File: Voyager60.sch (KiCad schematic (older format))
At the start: 261 parts, among them Q1 2N7002, SW1 5.2x5.2mm, U1 ATmega32U4-MU, U2 PRTR5V0U2X, Y1 16Mhz

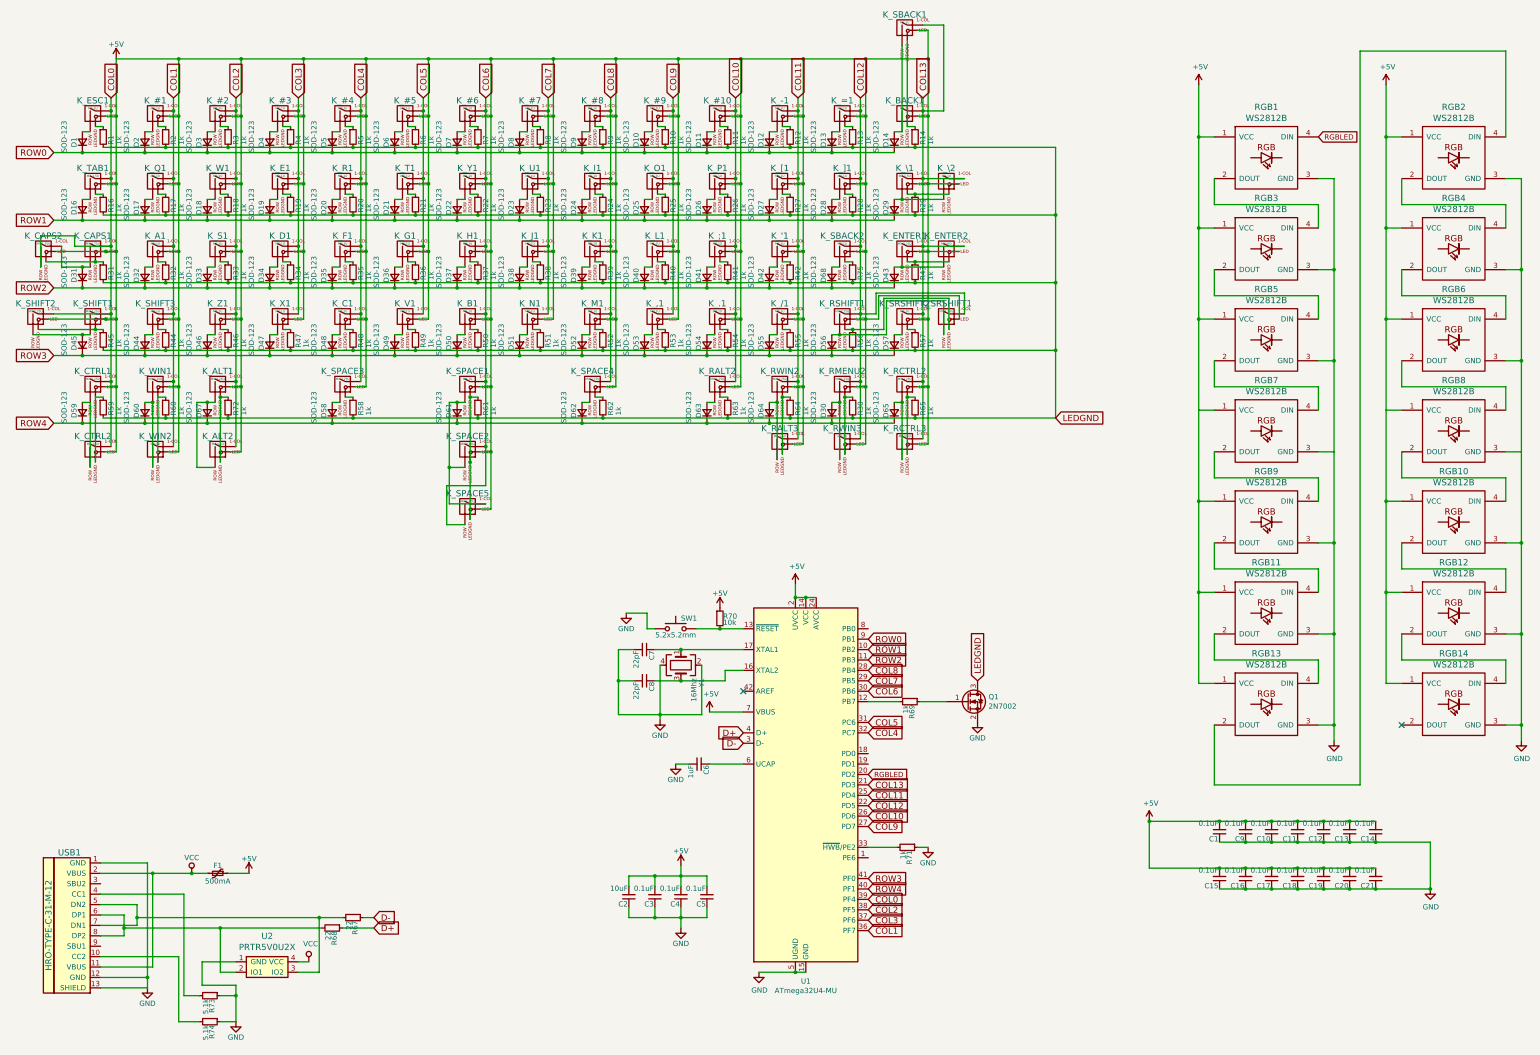
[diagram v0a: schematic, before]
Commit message: 65% variant of voyager60
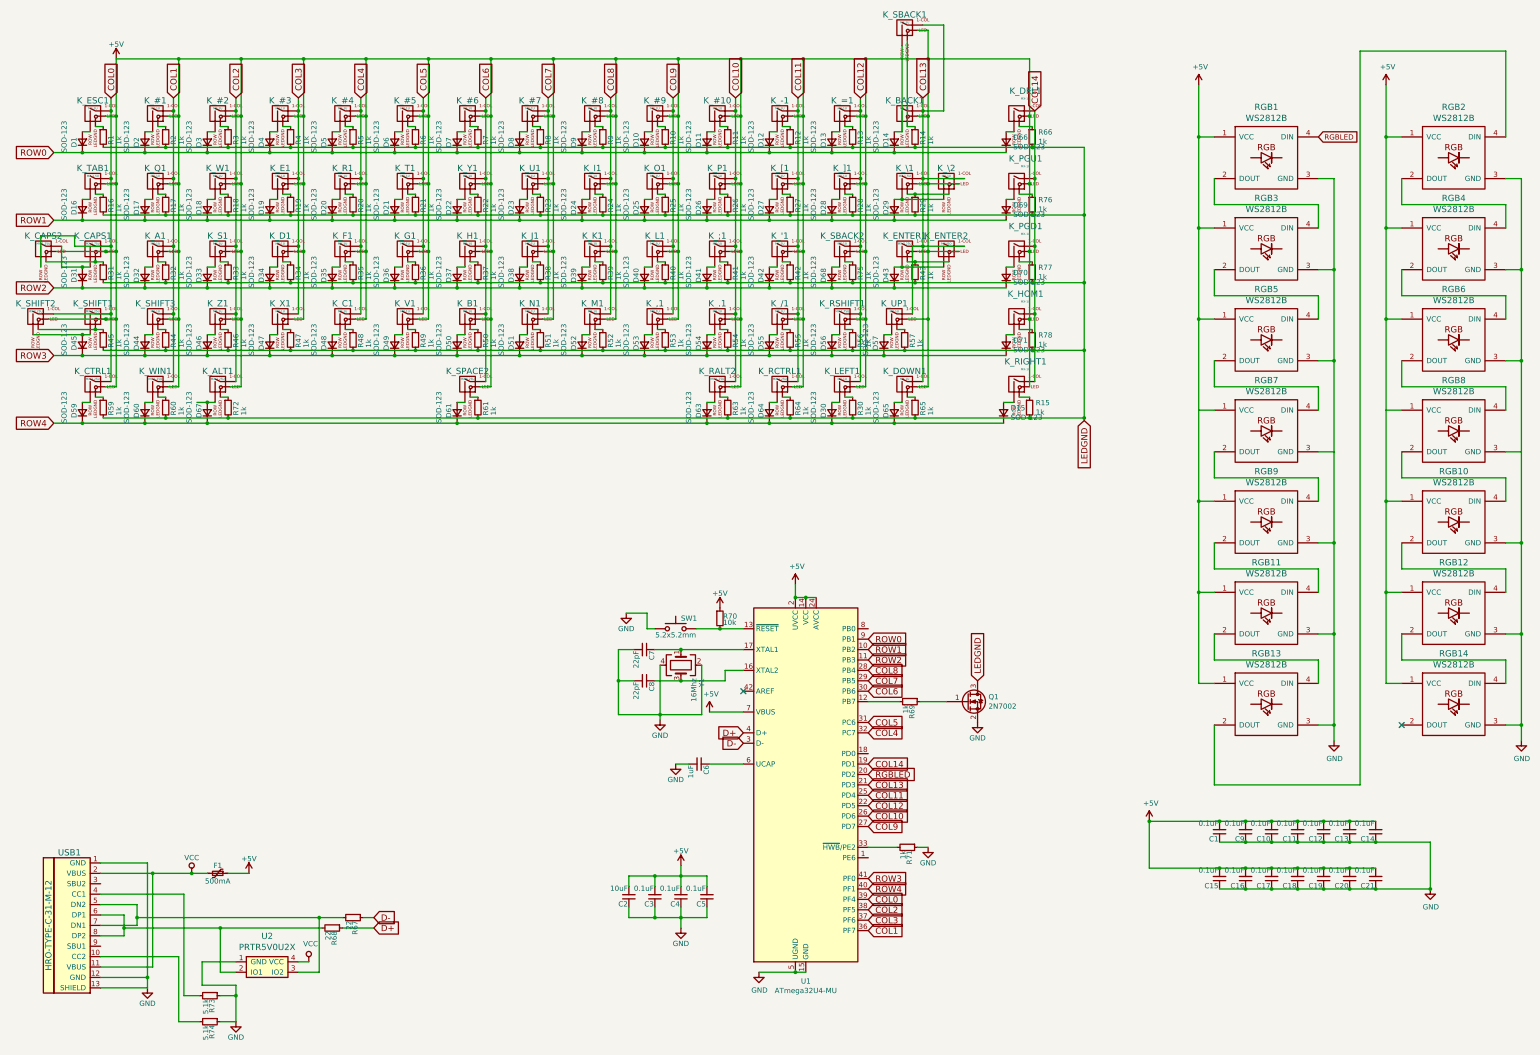
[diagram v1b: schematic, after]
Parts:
- removed D58, D62: SOD-123, Diodes_SMD:D_SOD-123, symbol Device:D_Small
- removed K_ALT2, K_CTRL2, K_RALT3, K_RCTRL3: MX-1.5U, MX_Alps_Hybrid:MX-1.5U-FLIPPED, symbol MX_Alps_Hybrids:MX-1U
- removed K_RWIN3, K_SRSHIFT2: MX-1U, MX_Alps_Hybrid:MX-1U, symbol MX_Alps_Hybrids:MX-1U
- removed K_SPACE1: MX-7U, MX_Alps_Hybrid:MX-7U-ReversedStabilizers, symbol MX_Alps_Hybrids:MX-1U
- removed K_SPACE3: MX-2.25U, MX_Alps_Hybrid:MX-2.25U-ReversedStabilizers, symbol MX_Alps_Hybrids:MX-1U
- removed K_SPACE4: MX-2.75U, MX_Alps_Hybrid:MX-2.75U-ReversedStabilizers, symbol MX_Alps_Hybrids:MX-1U
- removed K_SPACE5: MX-1.25U, MX_Alps_Hybrid:MX-1.25U-FLIPPED, symbol MX_Alps_Hybrids:MX-1U
- removed K_SRSHIFT1: MX-1.75U, MX_Alps_Hybrid:MX-1.75U, symbol MX_Alps_Hybrids:MX-1U
- removed K_WIN2: MX-1U, MX_Alps_Hybrid:MX-1U-FLIPPED, symbol MX_Alps_Hybrids:MX-1U
- removed R58, R62: 1k, Resistors_SMD:R_0805, symbol Device:R_Small
- added D15, D66, D69, D70, D71: SOD-123, Diodes_SMD:D_SOD-123, symbol Device:D_Small
- added K_DEL1, K_HOM1, K_PGD1, K_PGU1, K_RIGHT1, K_UP1: MX-1U, MX_Alps_Hybrid:MX-1U, symbol MX_Alps_Hybrids:MX-1U
- added R15, R66, R76, R77, R78: 1k, Resistors_SMD:R_0805, symbol Device:R_Small
- K_DOWN1: renamed from K_RCTRL2; value MX-1.25U -> MX-1U; footprint MX_Alps_Hybrid:MX-1.25U -> MX_Alps_Hybrid:MX-1U
- K_LEFT1: renamed from K_RMENU2; value MX-1.25U -> MX-1U; footprint MX_Alps_Hybrid:MX-1.25U-FLIPPED -> MX_Alps_Hybrid:MX-1U
- K_RSHIFT1: value MX-2.75U -> MX-1.75U; footprint MX_Alps_Hybrid:MX-2.75U-FLIPPED -> MX_Alps_Hybrid:MX-1.75U
- renumbered K_RWIN2 to K_RCTRL1
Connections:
- net +5V: now also K_DEL1.3 (LED), K_HOM1.3 (LED), K_PGD1.3 (LED), K_PGU1.3 (LED), K_RIGHT1.3 (LED), K_UP1.3 (LED)
- net COL13: now also K_UP1.1 (COL)
- net LEDGND: now also R15.2, R66.2, R76.2, R77.2, R78.2
- net ROW0: now also D66.1 (K)
- net ROW1: now also D69.1 (K)
- net ROW2: now also D70.1 (K)
- net ROW3: now also D71.1 (K)
- net ROW4: now also D15.1 (K)
- net at D57.2 (A): now also K_UP1.2 (ROW)
- net at R57.1: now also K_UP1.4 (LEDGND)
- net COL14: now reaches U1.19 (PD1)
- net COL14: now also K_DEL1.1 (COL), K_HOM1.1 (COL), K_PGD1.1 (COL), K_PGU1.1 (COL), K_RIGHT1.1 (COL)
- new net: D66.2 (A), K_DEL1.2 (ROW)
- new net: K_DEL1.4 (LEDGND), R66.1
- new net: D69.2 (A), K_PGU1.2 (ROW)
- new net: K_PGU1.4 (LEDGND), R76.1
- new net: D70.2 (A), K_PGD1.2 (ROW)
- new net: K_PGD1.4 (LEDGND), R77.1
- new net: D71.2 (A), K_HOM1.2 (ROW)
- new net: K_HOM1.4 (LEDGND), R78.1
- new net: D15.2 (A), K_RIGHT1.2 (ROW)
- new net: K_RIGHT1.4 (LEDGND), R15.1
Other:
- moved on the sheet: K_SPACE2
